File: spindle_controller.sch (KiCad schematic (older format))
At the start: 64 parts, among them J1 VAC 230V, J2 AUX/CONTROL, J3 ICP, J4 Load output, J5 CONN_01X03, J6 CONN_01X03, J7 GND_JUMPER, J8 VCC_JUMPER, J9 Jack_3.5mm_4pin, Q1 2N3904, SW1 Rotary_Encoder_Switch, T1 230 - 6VAC (Spitznagel SPK 01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, U1 LT1117-5, U2 LM2940CT-5.0, U3 ATMEGA328P-PU, U4 PC817, U5 MOC3020M, U6 TCRT5000, Y1 16MHz

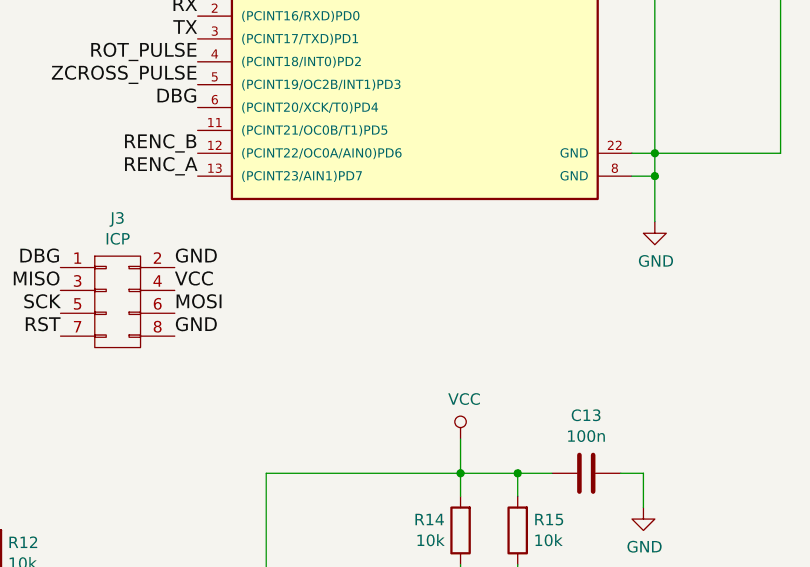
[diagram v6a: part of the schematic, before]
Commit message: Add reset button
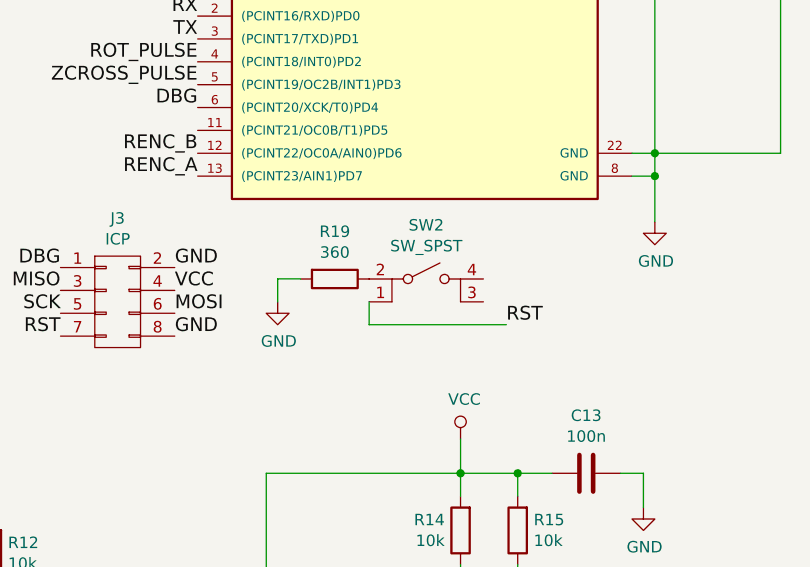
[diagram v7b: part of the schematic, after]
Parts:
- added R19: 360, Resistors_ThroughHole:R_Axial_DIN0204_L3.6mm_D1.6mm_P7.62mm_Horizontal, symbol R
- added SW2: SW_SPST, Buttons_Switches_ThroughHole:SW_PUSH_6mm, symbol SW_SPST
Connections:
- net GND: now also R19.2
- net RST: now also SW2.1
- new net: R19.1, SW2.2
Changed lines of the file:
@@
 	-1   0    0    1
+$EndComp
+$Comp
+L SW_SPST SW2
+U 1 1 59387C9F
+P 9300 3850
+F 0 "SW2" H 9300 4085 50  0000 C CNN
+F 1 "SW_SPST" H 9300 3994 50  0000 C CNN
+F 2 "Buttons_Switches_ThroughHole:SW_PUSH_6mm" H 9300 3850 50  0001 C CNN
+F 3 "" H 9300 3850 50  0001 C CNN
+	1    9300 3850
+	1    0    0    -1
+$EndComp
+$Comp
+L R R19
+U 1 1 59387E1D
+P 8900 3850
+F 0 "R19" V 8693 3850 50  0000 C CNN
+F 1 "360" V 8784 3850 50  0000 C CNN
+F 2 "Resistors_ThroughHole:R_Axial_DIN0204_L3.6mm_D1.6mm_P7.62mm_Horizontal" V 8830 3850 50  0001 C CNN
+F 3 "" H 8900 3850 50  0001 C CNN
+	1    8900 3850
+	0    1    1    0
+$EndComp
+$Comp
+L GND #PWR021
+U 1 1 59387EFB
+P 8650 3950
+F 0 "#PWR021" H 8650 3700 50  0001 C CNN
+F 1 "GND" H 8655 3777 50  0000 C CNN
+F 2 "" H 8650 3950 50  0001 C CNN
+F 3 "" H 8650 3950 50  0001 C CNN
+	1    8650 3950
+	1    0    0    -1
 $EndComp
 Wire Wire Line
@@
 Wire Wire Line
 	8600 5350 8700 5350
+Text Label 9650 4050 0    60   ~ 0
+RST
+Wire Wire Line
+	9050 3950 9050 4050
+Wire Wire Line
+	9050 4050 9650 4050
+Wire Wire Line
+	8650 3950 8650 3850
+Wire Wire Line
+	8650 3850 8750 3850
 $EndSCHEMATC
